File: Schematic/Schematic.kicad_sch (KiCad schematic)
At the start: 1 part, among them U1 STM32F091RCT6

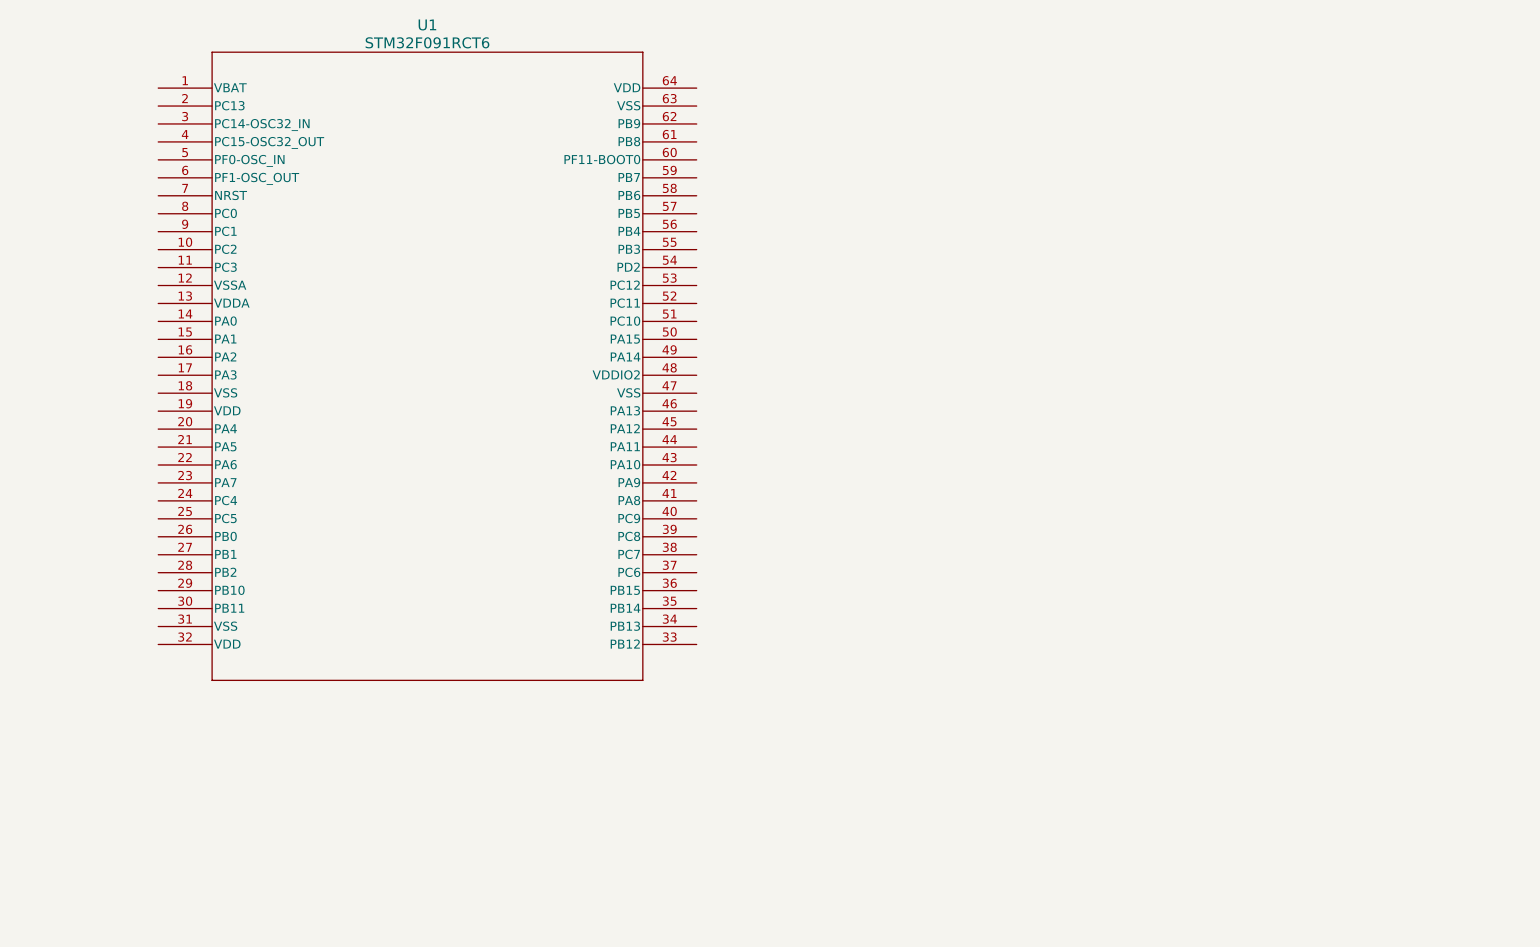
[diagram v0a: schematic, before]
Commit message: Added paritial schematic including microprocessor, hub75 and keypad
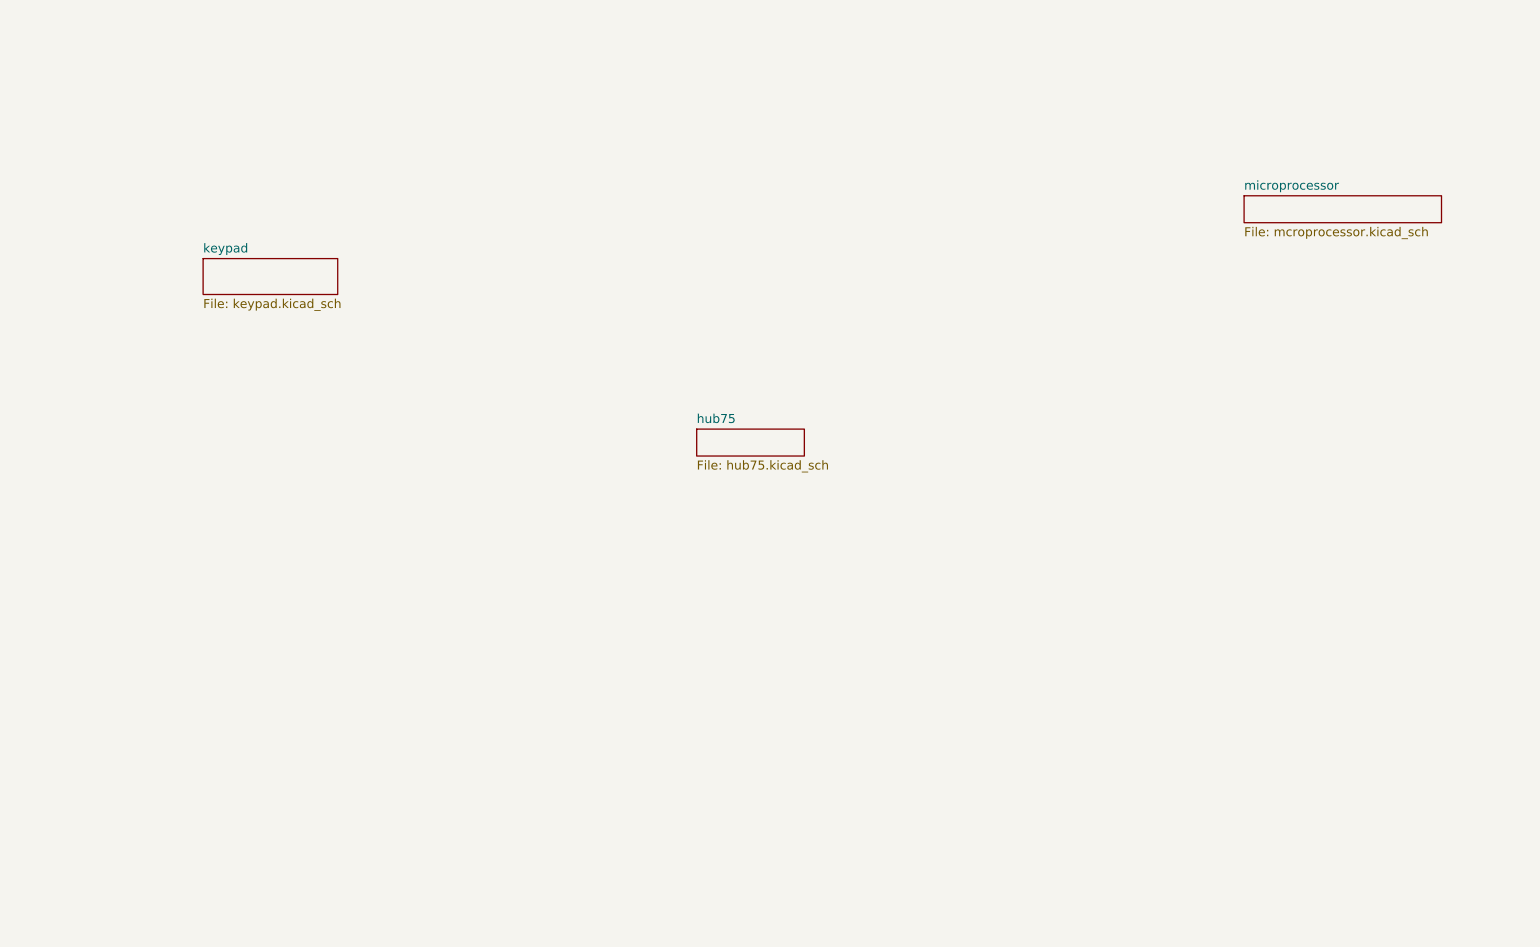
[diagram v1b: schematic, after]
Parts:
- removed U1: STM32F091RCT6, STM32F091RCT6:LQFP64-10x10mm_STM, symbol STM32F091RCT6:STM32F091RCT6
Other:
- added sheet hub75 (hub75.kicad_sch)
- added sheet keypad (keypad.kicad_sch)
- added sheet microprocessor (mcroprocessor.kicad_sch)
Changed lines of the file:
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@@
 (kicad_sch (version 20230121) (generator eeschema)
   (paper "A4")
-  (symbol (lib_id "STM32F091RCT6:STM32F091RCT6") (at 73.66 26.67 0) (unit 1)
-    (in_bom yes) (on_board yes) (dnp no) (fields_autoplaced)
-    (property "Reference" "U1" (at 111.76 17.78 0)
-      (effects (font (size 1.524 1.524)))
+  (sheet (at 149.86 74.93) (size 15.24 3.81) (fields_autoplaced)
+    (stroke (width 0.1524) (type solid))
+    (fill (color 0 0 0 0.0000))
+    (property "Sheetname" "hub75" (at 149.86 74.2184 0)
+      (effects (font (size 1.27 1.27)) (justify left bottom))
     )
-    (property "Value" "STM32F091RCT6" (at 111.76 20.32 0)
-      (effects (font (size 1.524 1.524)))
+    (property "Sheetfile" "hub75.kicad_sch" (at 149.86 79.3246 0)
+      (effects (font (size 1.27 1.27)) (justify left top))
     )
-    (property "Footprint" "STM32F091RCT6:LQFP64-10x10mm_STM" (at 73.66 26.67 0)
-      (effects (font (size 1.27 1.27) italic) hide)
-    )
-    (property "Datasheet" "STM32F091RCT6" (at 73.66 26.67 0)
-      (effects (font (size 1.27 1.27) italic) hide)
-    )
-    (pin "1")
-    (pin "10")
-    (pin "11")
-    (pin "12")
-    (pin "13")
-    (pin "14")
-    (pin "15")
-    (pin "16")
-    (pin "17")
-    (pin "18")
-    (pin "19")
-    (pin "2")
-    (pin "20")
-    (pin "21")
-    (pin "22")
-    (pin "23")
-    (pin "24")
-    (pin "25")
-    (pin "26")
-    (pin "27")
-    (pin "28")
-    (pin "29")
-    (pin "3")
-    (pin "30")
-    (pin "31")
-    (pin "32")
-    (pin "33")
-    (pin "34")
-    (pin "35")
-    (pin "36")
-    (pin "37")
-    (pin "38")
-    (pin "39")
-    (pin "4")
-    (pin "40")
-    (pin "41")
-    (pin "42")
-    (pin "43")
-    (pin "44")
-    (pin "45")
-    (pin "46")
-    (pin "47")
-    (pin "48")
-    (pin "49")
-    (pin "5")
-    (pin "50")
-    (pin "51")
-    (pin "52")
-    (pin "53")
-    (pin "54")
-    (pin "55")
-    (pin "56")
-    (pin "57")
-    (pin "58")
-    (pin "59")
-    (pin "6")
-    (pin "60")
-    (pin "61")
-    (pin "62")
-    (pin "63")
-    (pin "64")
-    (pin "7")
-    (pin "8")
-    (pin "9")
     (instances
       (project "Schematic"
-        (path "/ced54cd9-3b34-40e4-aa66-964aaab81b0a"
-          (reference "U1") (unit 1)
-        )
+        (path "/ced54cd9-3b34-40e4-aa66-964aaab81b0a" (page "3"))
       )
     )
+  )
+  (sheet (at 227.33 41.91) (size 27.94 3.81) (fields_autoplaced)
+    (stroke (width 0.1524) (type solid))
+    (fill (color 0 0 0 0.0000))
+    (property "Sheetname" "microprocessor" (at 227.33 41.1984 0)
+      (effects (font (size 1.27 1.27)) (justify left bottom))
+    )
+    (property "Sheetfile" "mcroprocessor.kicad_sch" (at 227.33 46.3046 0)
+      (effects (font (size 1.27 1.27)) (justify left top))
+    )
+    (instances
+      (project "Schematic"
+        (path "/ced54cd9-3b34-40e4-aa66-964aaab81b0a" (page "2"))
+      )
+    )
+  )
+  (sheet (at 80.01 50.8) (size 19.05 5.08) (fields_autoplaced)
+    (stroke (width 0.1524) (type solid))
+    (fill (color 0 0 0 0.0000))
+    (property "Sheetname" "keypad" (at 80.01 50.0884 0)
+      (effects (font (size 1.27 1.27)) (justify left bottom))
+    )
+    (property "Sheetfile" "keypad.kicad_sch" (at 80.01 56.4646 0)
+      (effects (font (size 1.27 1.27)) (justify left top))
+    )
+    (instances
+      (project "Schematic"
+        (path "/ced54cd9-3b34-40e4-aa66-964aaab81b0a" (page "4"))
+      )
+    )

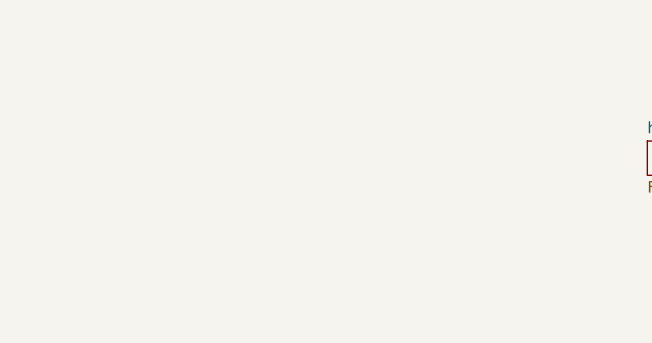
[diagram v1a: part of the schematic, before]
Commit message: Added audio circuitry
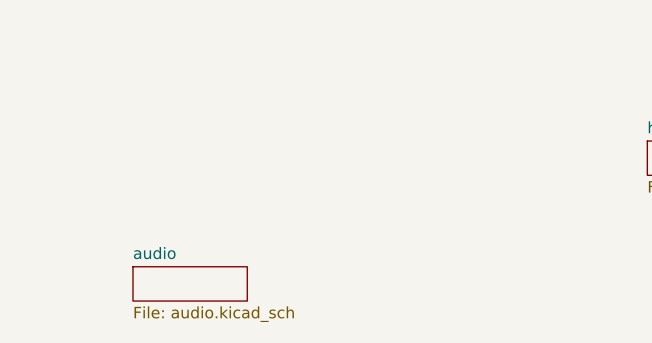
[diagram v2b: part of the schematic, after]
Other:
- added sheet audio (audio.kicad_sch)
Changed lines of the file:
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@@
+    )
+  )
+  (sheet (at 92.71 88.9) (size 12.7 3.81) (fields_autoplaced)
+    (stroke (width 0.1524) (type solid))
+    (fill (color 0 0 0 0.0000))
+    (property "Sheetname" "audio" (at 92.71 88.1884 0)
+      (effects (font (size 1.27 1.27)) (justify left bottom))
+    )
+    (property "Sheetfile" "audio.kicad_sch" (at 92.71 93.2946 0)
+      (effects (font (size 1.27 1.27)) (justify left top))
+    )
+    (instances
+      (project "Schematic"
+        (path "/ced54cd9-3b34-40e4-aa66-964aaab81b0a" (page "5"))
+      )
     )
   )

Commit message: initial CB design
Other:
- added sheet power (power.kicad_sch)
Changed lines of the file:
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@@
+    )
+  )
+  (sheet (at 57.15 118.11) (size 12.7 3.81) (fields_autoplaced)
+    (stroke (width 0.1524) (type solid))
+    (fill (color 0 0 0 0.0000))
+    (property "Sheetname" "power" (at 57.15 117.3984 0)
+      (effects (font (size 1.27 1.27)) (justify left bottom))
+    )
+    (property "Sheetfile" "power.kicad_sch" (at 57.15 122.5046 0)
+      (effects (font (size 1.27 1.27)) (justify left top))
+    )
+    (instances
+      (project "Schematic"
+        (path "/ced54cd9-3b34-40e4-aa66-964aaab81b0a" (page "6"))
+      )
     )
   )

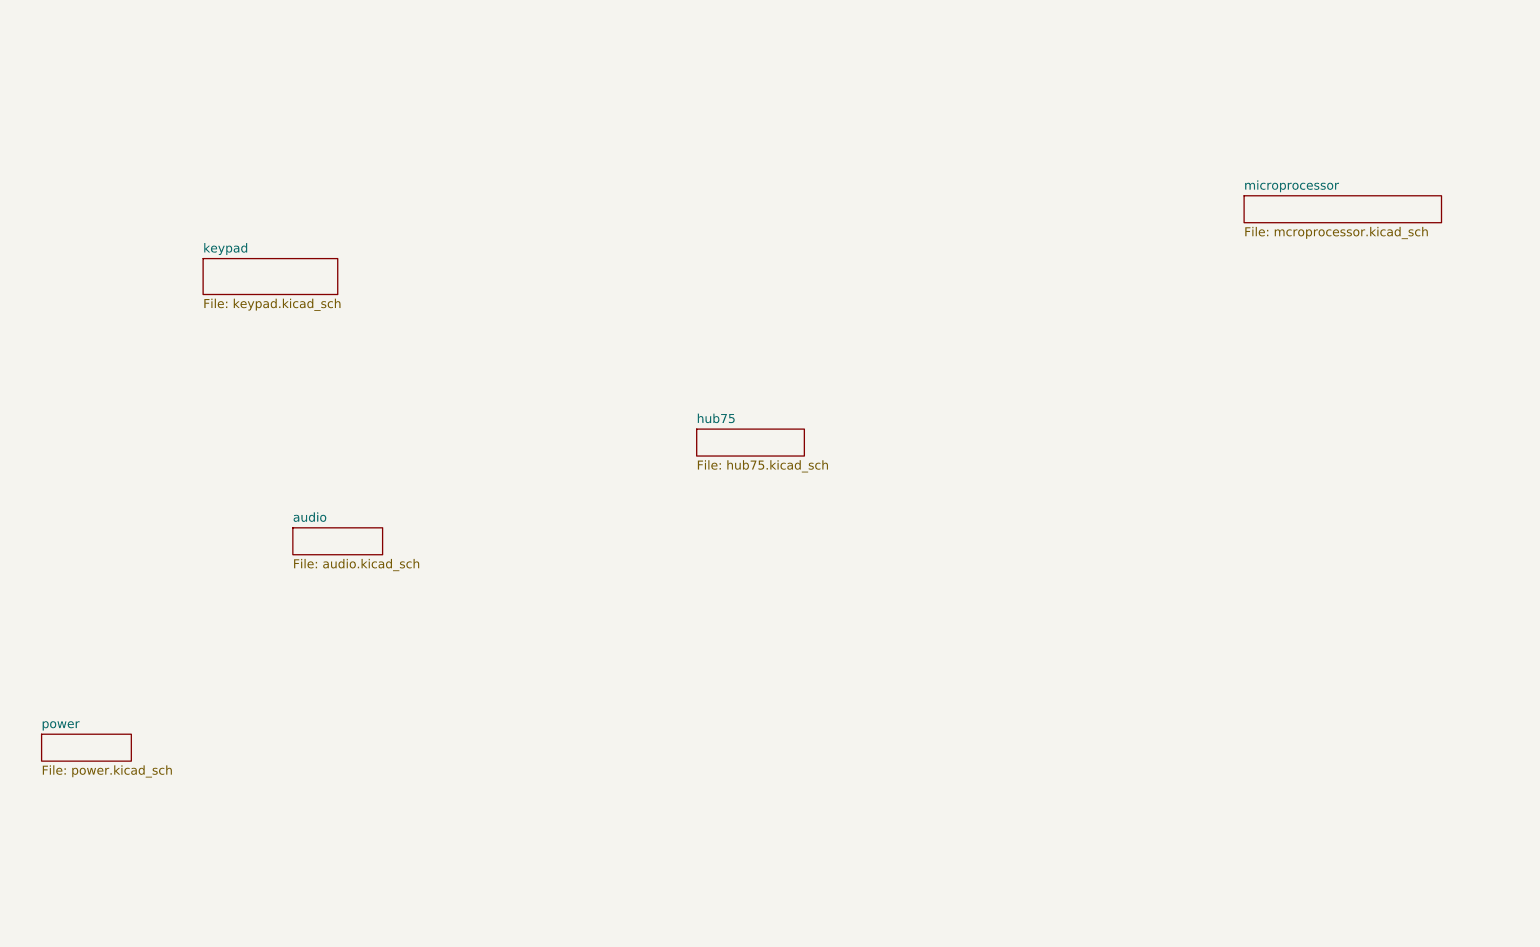
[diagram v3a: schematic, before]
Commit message: Most of the schematic and PCB layout.
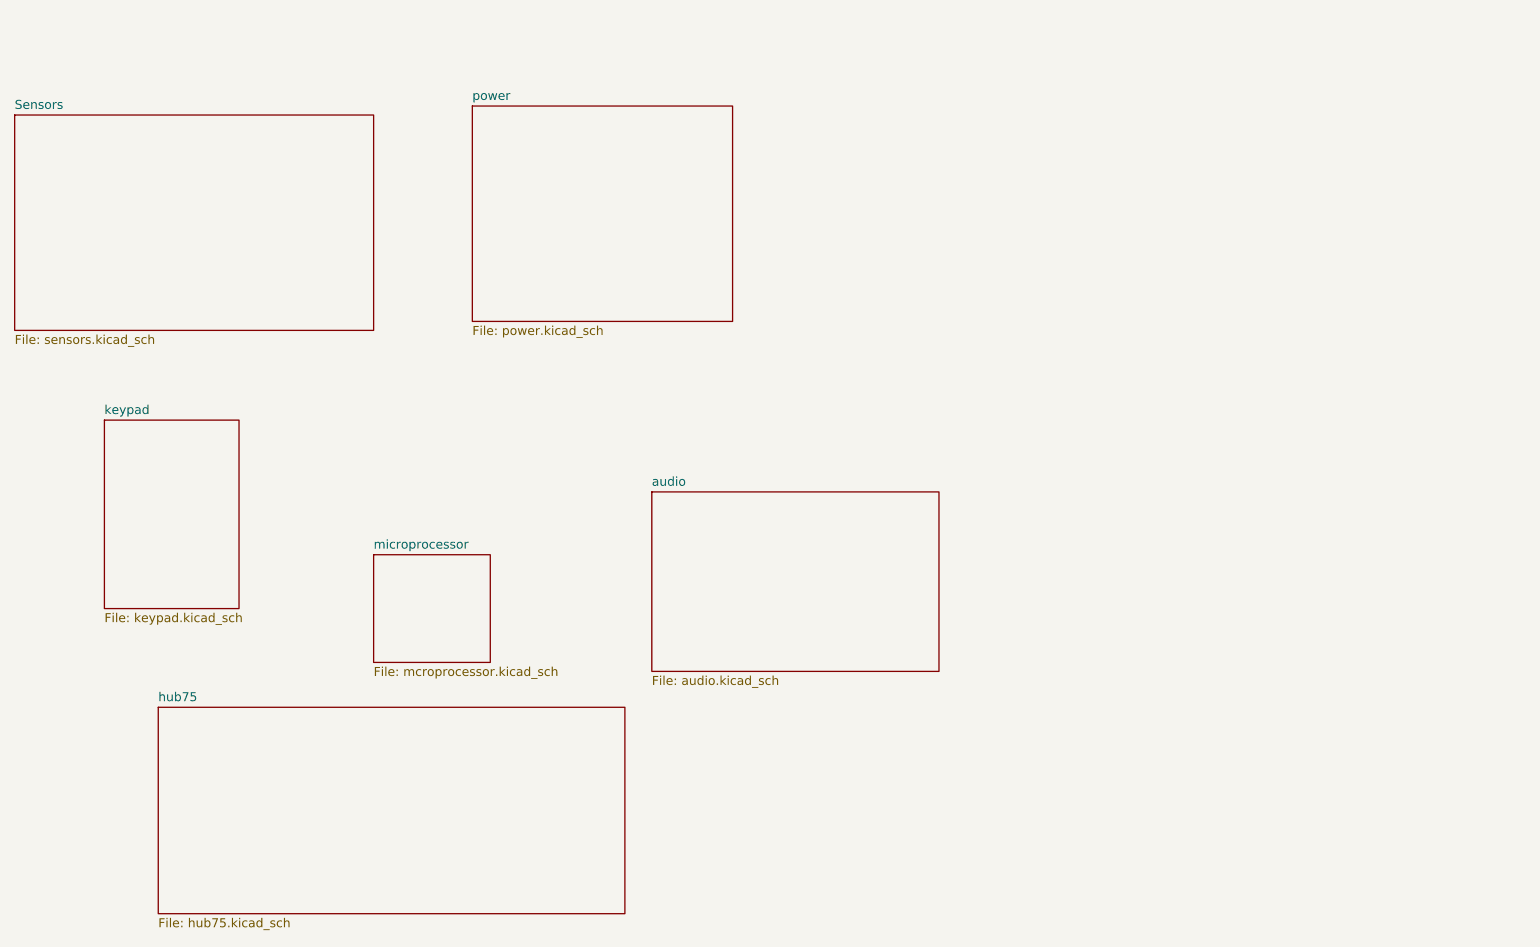
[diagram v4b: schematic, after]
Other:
- added sheet Sensors (sensors.kicad_sch)
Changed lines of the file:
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@@
 (kicad_sch (version 20230121) (generator eeschema)
   (paper "A4")
-  (sheet (at 149.86 74.93) (size 15.24 3.81) (fields_autoplaced)
+  (sheet (at 73.66 114.3) (size 66.04 29.21) (fields_autoplaced)
     (stroke (width 0.1524) (type solid))
     (fill (color 0 0 0 0.0000))
-    (property "Sheetname" "hub75" (at 149.86 74.2184 0)
+    (property "Sheetname" "hub75" (at 73.66 113.5884 0)
       (effects (font (size 1.27 1.27)) (justify left bottom))
     )
-    (property "Sheetfile" "hub75.kicad_sch" (at 149.86 79.3246 0)
+    (property "Sheetfile" "hub75.kicad_sch" (at 73.66 144.0946 0)
       (effects (font (size 1.27 1.27)) (justify left top))
     )
@@
     )
   )
-  (sheet (at 57.15 118.11) (size 12.7 3.81) (fields_autoplaced)
+  (sheet (at 118.11 29.21) (size 36.83 30.48) (fields_autoplaced)
     (stroke (width 0.1524) (type solid))
     (fill (color 0 0 0 0.0000))
-    (property "Sheetname" "power" (at 57.15 117.3984 0)
+    (property "Sheetname" "power" (at 118.11 28.4984 0)
       (effects (font (size 1.27 1.27)) (justify left bottom))
     )
-    (property "Sheetfile" "power.kicad_sch" (at 57.15 122.5046 0)
+    (property "Sheetfile" "power.kicad_sch" (at 118.11 60.2746 0)
       (effects (font (size 1.27 1.27)) (justify left top))
     )
@@
     )
   )
-  (sheet (at 92.71 88.9) (size 12.7 3.81) (fields_autoplaced)
+  (sheet (at 143.51 83.82) (size 40.64 25.4) (fields_autoplaced)
     (stroke (width 0.1524) (type solid))
     (fill (color 0 0 0 0.0000))
-    (property "Sheetname" "audio" (at 92.71 88.1884 0)
+    (property "Sheetname" "audio" (at 143.51 83.1084 0)
       (effects (font (size 1.27 1.27)) (justify left bottom))
     )
-    (property "Sheetfile" "audio.kicad_sch" (at 92.71 93.2946 0)
+    (property "Sheetfile" "audio.kicad_sch" (at 143.51 109.8046 0)
       (effects (font (size 1.27 1.27)) (justify left top))
     )
@@
     )
   )
-  (sheet (at 227.33 41.91) (size 27.94 3.81) (fields_autoplaced)
+  (sheet (at 104.14 92.71) (size 16.51 15.24) (fields_autoplaced)
     (stroke (width 0.1524) (type solid))
     (fill (color 0 0 0 0.0000))
-    (property "Sheetname" "microprocessor" (at 227.33 41.1984 0)
+    (property "Sheetname" "microprocessor" (at 104.14 91.9984 0)
       (effects (font (size 1.27 1.27)) (justify left bottom))
     )
-    (property "Sheetfile" "mcroprocessor.kicad_sch" (at 227.33 46.3046 0)
+    (property "Sheetfile" "mcroprocessor.kicad_sch" (at 104.14 108.5346 0)
       (effects (font (size 1.27 1.27)) (justify left top))
     )
@@
     )
   )
-  (sheet (at 80.01 50.8) (size 19.05 5.08) (fields_autoplaced)
+  (sheet (at 53.34 30.48) (size 50.8 30.48) (fields_autoplaced)
     (stroke (width 0.1524) (type solid))
     (fill (color 0 0 0 0.0000))
-    (property "Sheetname" "keypad" (at 80.01 50.0884 0)
+    (property "Sheetname" "Sensors" (at 53.34 29.7684 0)
       (effects (font (size 1.27 1.27)) (justify left bottom))
     )
-    (property "Sheetfile" "keypad.kicad_sch" (at 80.01 56.4646 0)
+    (property "Sheetfile" "sensors.kicad_sch" (at 53.34 61.5446 0)
       (effects (font (size 1.27 1.27)) (justify left top))
     )
+    (instances
+      (project "Schematic"
+        (path "/ced54cd9-3b34-40e4-aa66-964aaab81b0a" (page "7"))
+      )
+    )
+  )
+  (sheet (at 66.04 73.66) (size 19.05 26.67) (fields_autoplaced)
+    (stroke (width 0.1524) (type solid))
+    (fill (color 0 0 0 0.0000))
+    (property "Sheetname" "keypad" (at 66.04 72.9484 0)
+      (effects (font (size 1.27 1.27)) (justify left bottom))
+    )
+    (property "Sheetfile" "keypad.kicad_sch" (at 66.04 100.9146 0)
+      (effects (font (size 1.27 1.27)) (justify left top))
+    )
